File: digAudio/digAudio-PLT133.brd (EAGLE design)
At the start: 18.4 x 37.5 mm, 12 parts

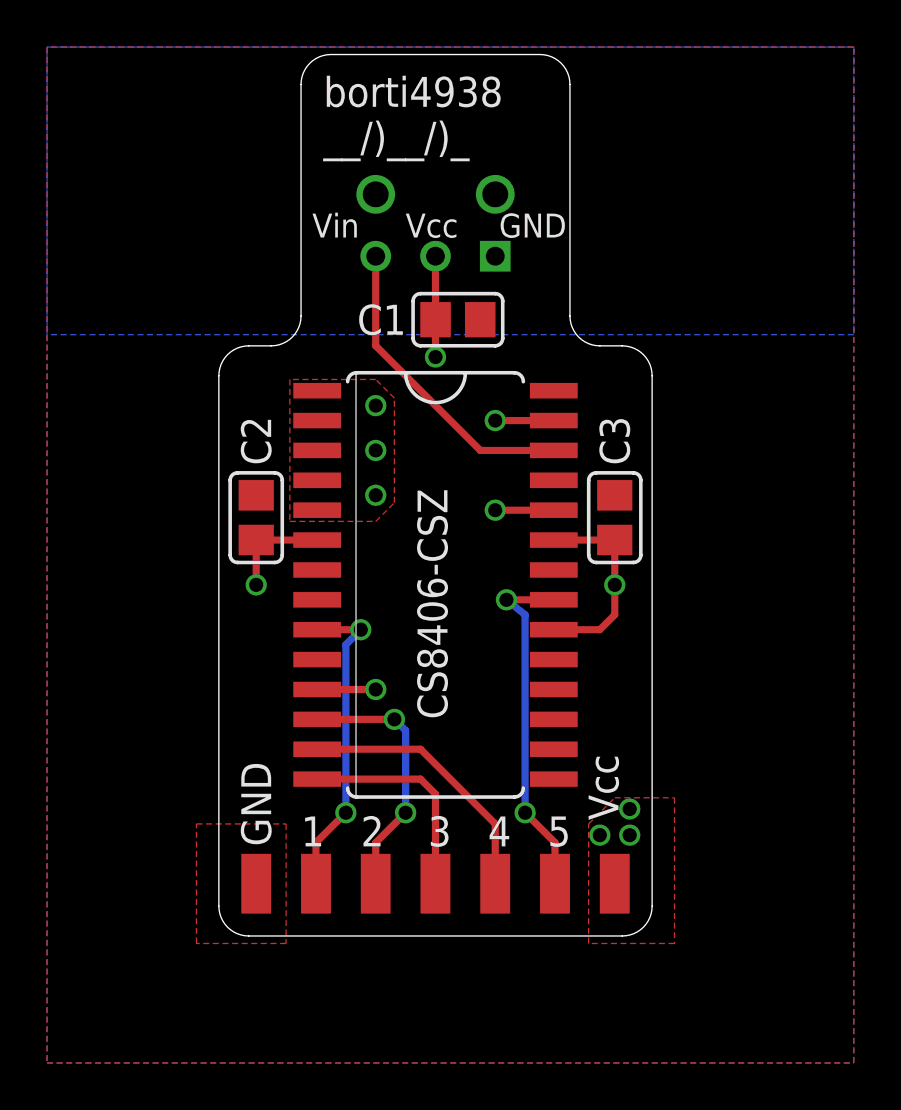
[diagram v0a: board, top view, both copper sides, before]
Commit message: update design: move GND pad
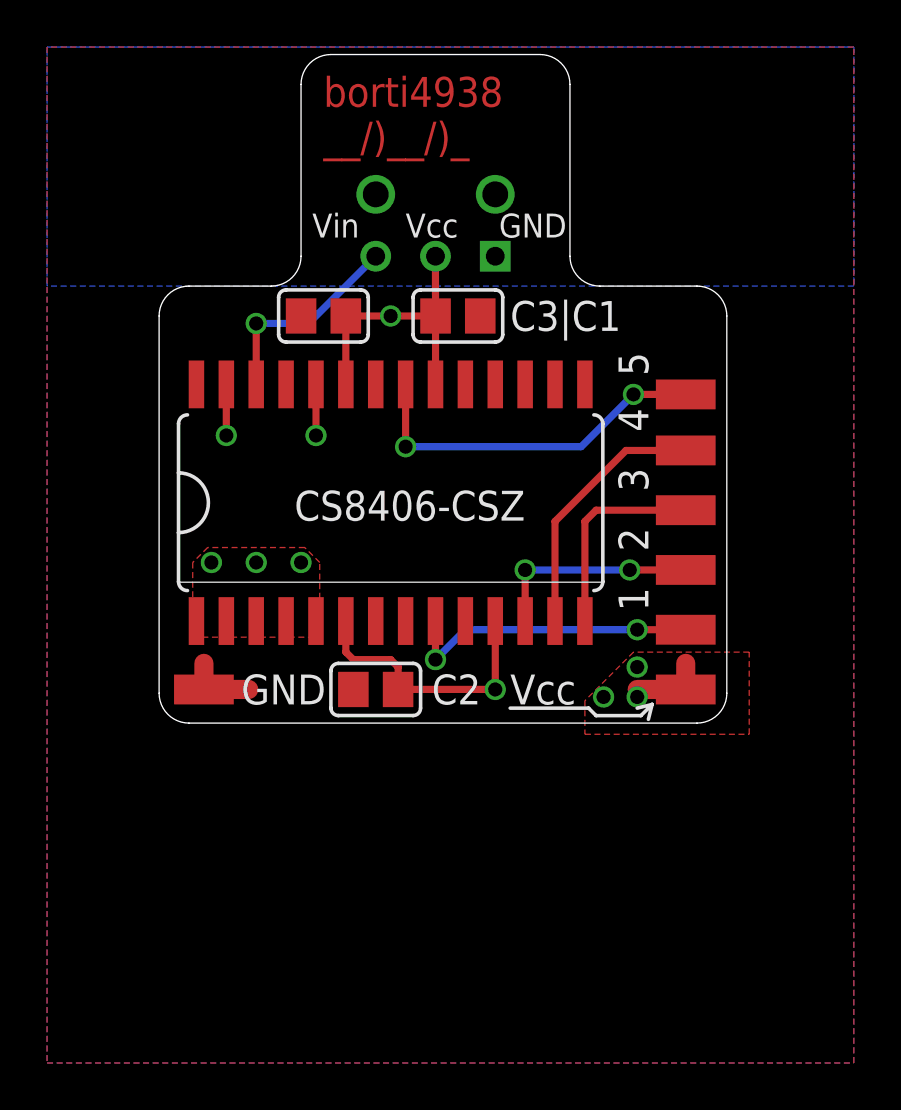
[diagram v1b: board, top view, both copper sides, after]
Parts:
- moved PAD5 21.5 mm to (27.1, 28.4), turned to 90 degrees
- moved PAD4 20.1 mm to (27.1, 26.0), turned to 90 degrees
- moved PAD3 19.1 mm to (27.1, 23.5), turned to 90 degrees
- moved PAD1 19.1 mm to (27.1, 18.4), turned to 90 degrees
- moved PAD2 18.7 mm to (27.1, 21.0), turned to 90 degrees
- moved U$4 15.1 mm to (11.7, 31.8), turned to 180 degrees
- moved U$3 8.90 mm to (14.0, 15.9), turned to 180 degrees
- moved VCC 8.79 mm to (27.1, 15.9), turned to 90 degrees
- moved GND 8.55 mm to (6.67, 15.9), turned to 270 degrees
- moved U$1 3.88 mm to (13.3, 23.8), turned to 0 degrees
- moved U$5 0.16 mm to (17.5, 31.8)
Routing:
- net VCC: track 25.2 -> 31.5 mm, vias 12 -> 10
- net N$1: track 13.2 -> 8.85 mm, vias 0 -> 1
- net GND: track 0.00 -> 3.02 mm
- net N$3: track 11.0 -> 9.00 mm
- net N$2: track 13.4 -> 12.8 mm
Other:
- board size 18.4 x 37.5 mm -> 24.1 x 28.4 mm
- board text added: ")"
- board text added: "/"
- board text added: "8"
- board text added: "9"
- board text added: "C3|C1"
- board text added: "Digital Audio Mod for SNES (Mini/Jr.)"
- board text added: "_"
- board text added: "b"
- board text added: "i"
- board text added: "o"
- board text added: "r"
- board text added: "t"
- board text removed: "C1"
- board text removed: "C3"
- board text removed: "Digital Audio Mod for SNES"
- board text removed: "PCB-Design by borti4938__/)_/)_"
